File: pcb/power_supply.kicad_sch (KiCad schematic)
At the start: 19 parts, among them J8 Screw_Terminal_01x02, Q1 Si2301, U2 LP2950ACZ-9.0, U3 AP2112K-3.3

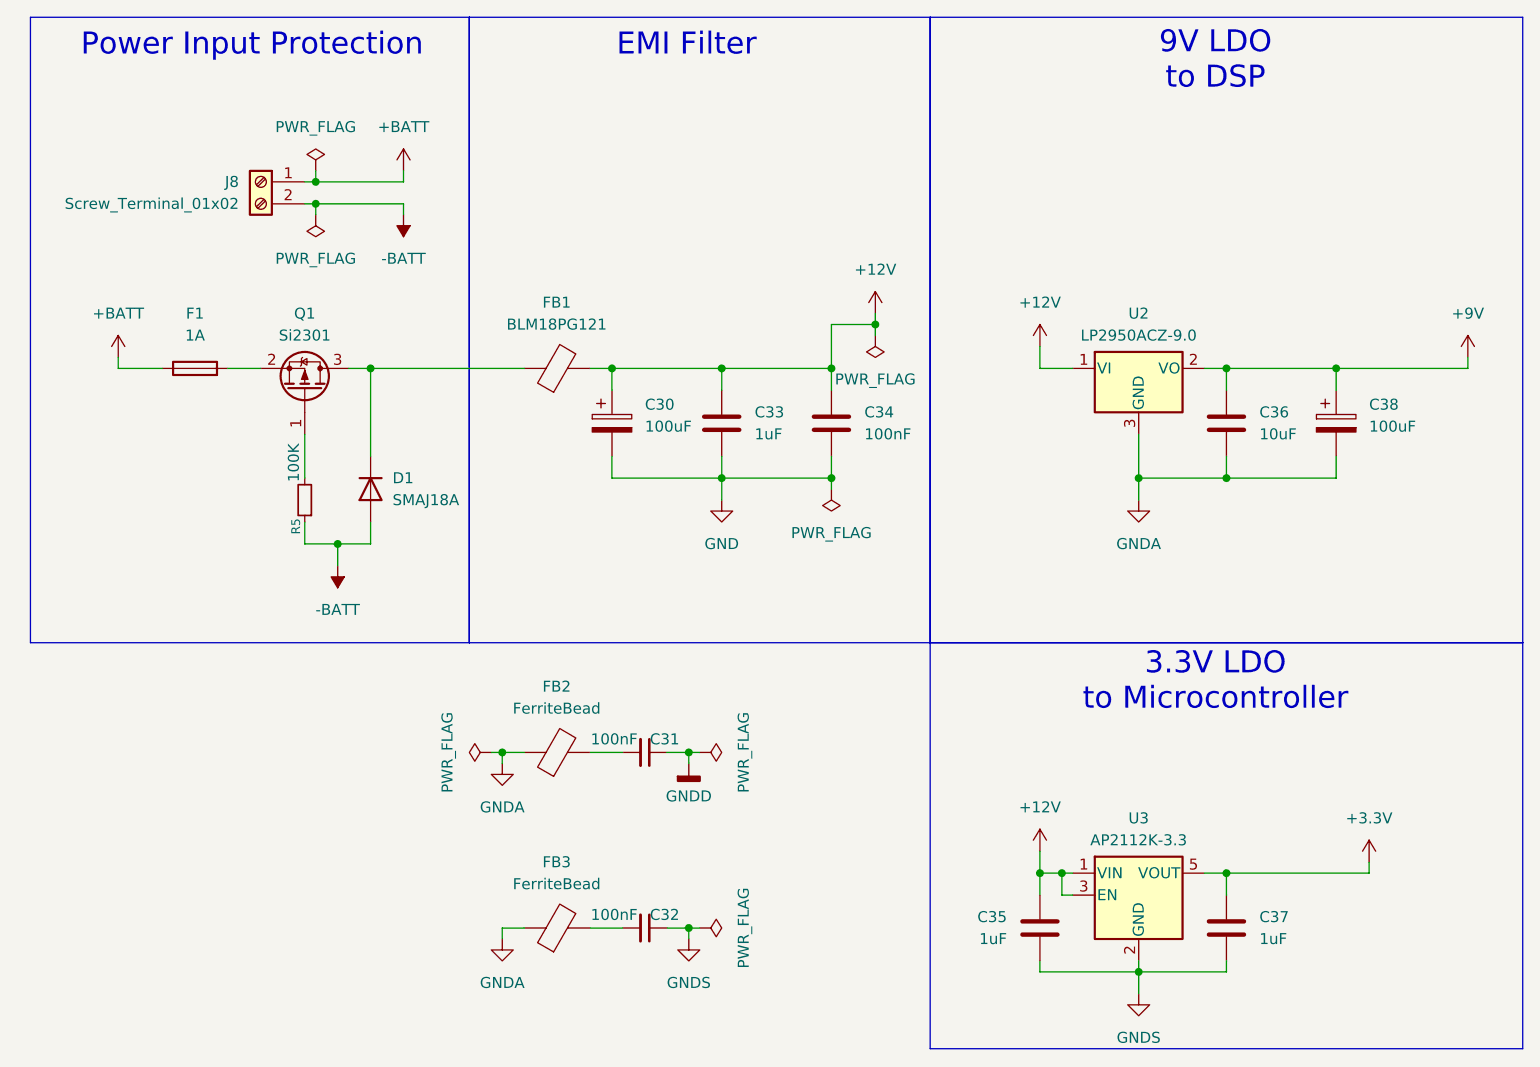
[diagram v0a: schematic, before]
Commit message: tweak schematic, add i2c pullup resistors.
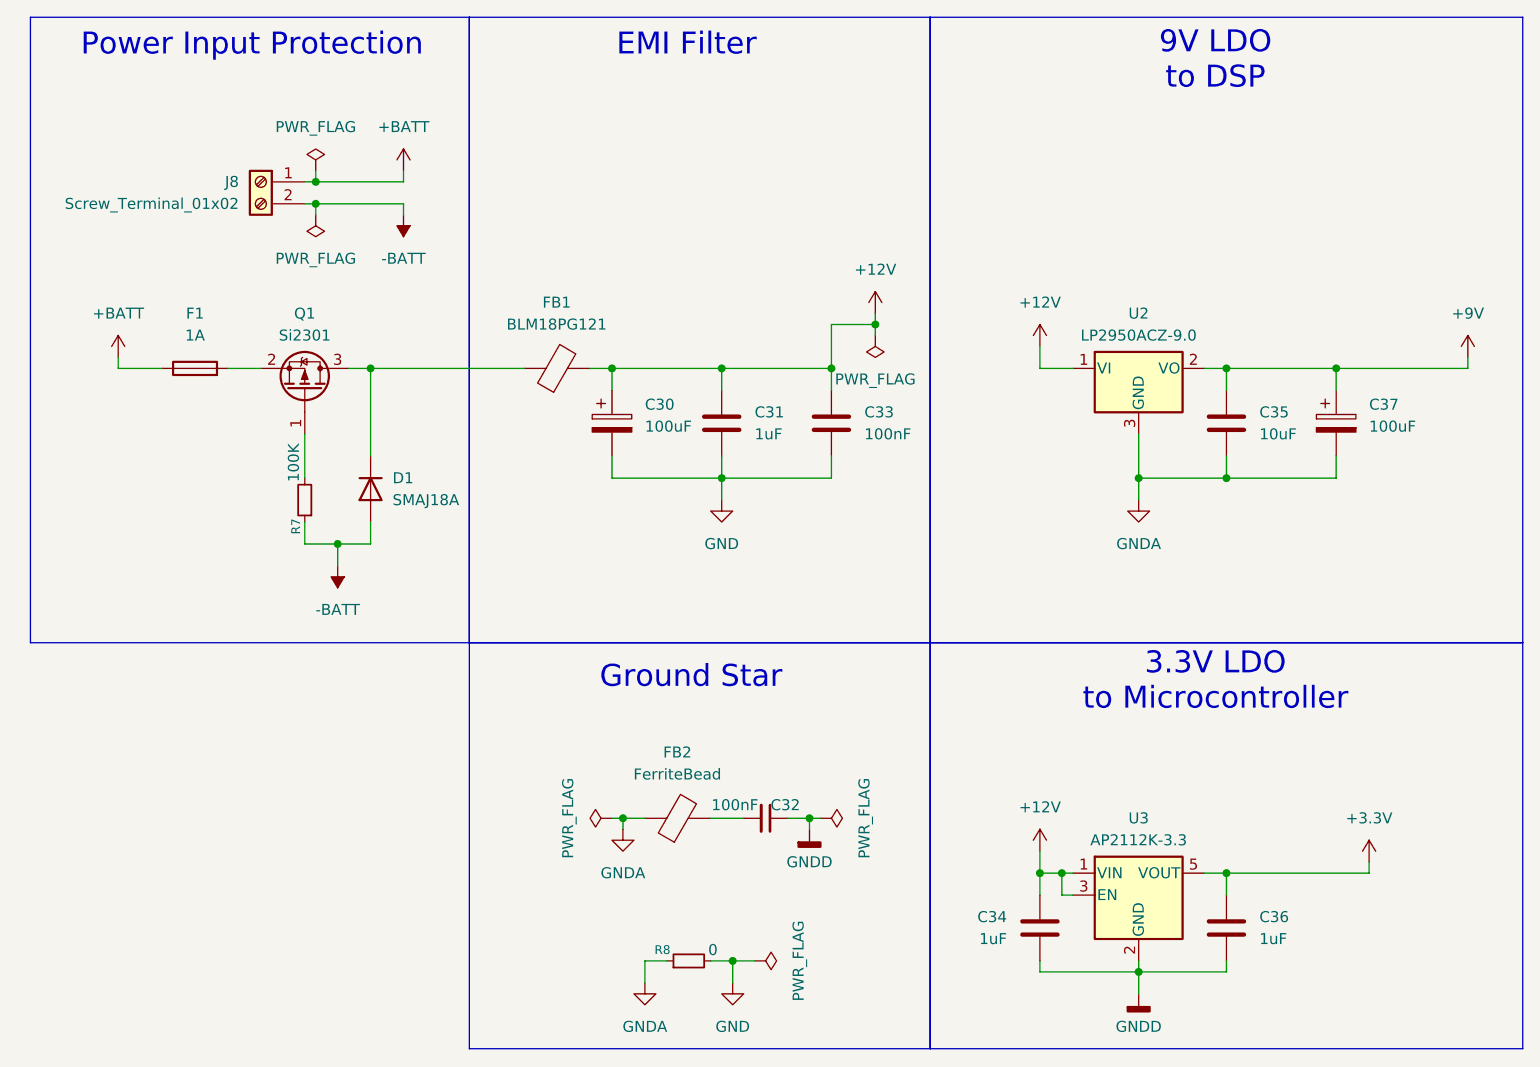
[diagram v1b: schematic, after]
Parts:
- removed C32: 100nF, symbol Device:C_Small
- removed FB3: FerriteBead, symbol Device:FerriteBead
- added R8: 0, symbol Device:R_Small
- C30: footprint (none) -> Capacitor_SMD:CP_Elec_10x10
- C31: renamed from C33; footprint (none) -> Capacitor_SMD:C_0805_2012Metric_Pad1.18x1.45mm_HandSolder
- C32: renamed from C31; footprint (none) -> Capacitor_SMD:C_0805_2012Metric
- C33: renamed from C34; footprint (none) -> Capacitor_SMD:C_0805_2012Metric_Pad1.18x1.45mm_HandSolder
- C34: renamed from C35; footprint (none) -> Capacitor_SMD:C_0805_2012Metric_Pad1.18x1.45mm_HandSolder
- C35: renamed from C36; footprint (none) -> Capacitor_SMD:C_0805_2012Metric_Pad1.18x1.45mm_HandSolder
- C36: renamed from C37; footprint (none) -> Capacitor_SMD:C_0805_2012Metric_Pad1.18x1.45mm_HandSolder
- C37: renamed from C38; footprint (none) -> Capacitor_SMD:CP_Elec_10x10
- D1: footprint (none) -> Diode_SMD:D_0805_2012Metric_Pad1.15x1.40mm_HandSolder
- F1: footprint (none) -> Fuse:Fuse_0805_2012Metric_Pad1.15x1.40mm_HandSolder
- FB1, FB2: footprint (none) -> Inductor_SMD:L_0805_2012Metric_Pad1.05x1.20mm_HandSolder
- renumbered R5 to R7
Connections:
- net GNDS is gone; now on net GNDD: C34.2, C36.2, U3.2 (GND)
- net GND: now also R8.2
- net GNDA: now also R8.1
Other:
- note added: "Ground Star"
- moved on the sheet: C32, FB2
